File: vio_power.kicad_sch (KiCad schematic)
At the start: 55 parts, among them J29 292161-3, U41 TCA6408ARGTR, U42 AZ1117H-1.8TRE1_SOT223, U43 LP2985-3.3, U44 MCP4728, U45 TPS7A4501DCQR, U46 TPS7A4501DCQR

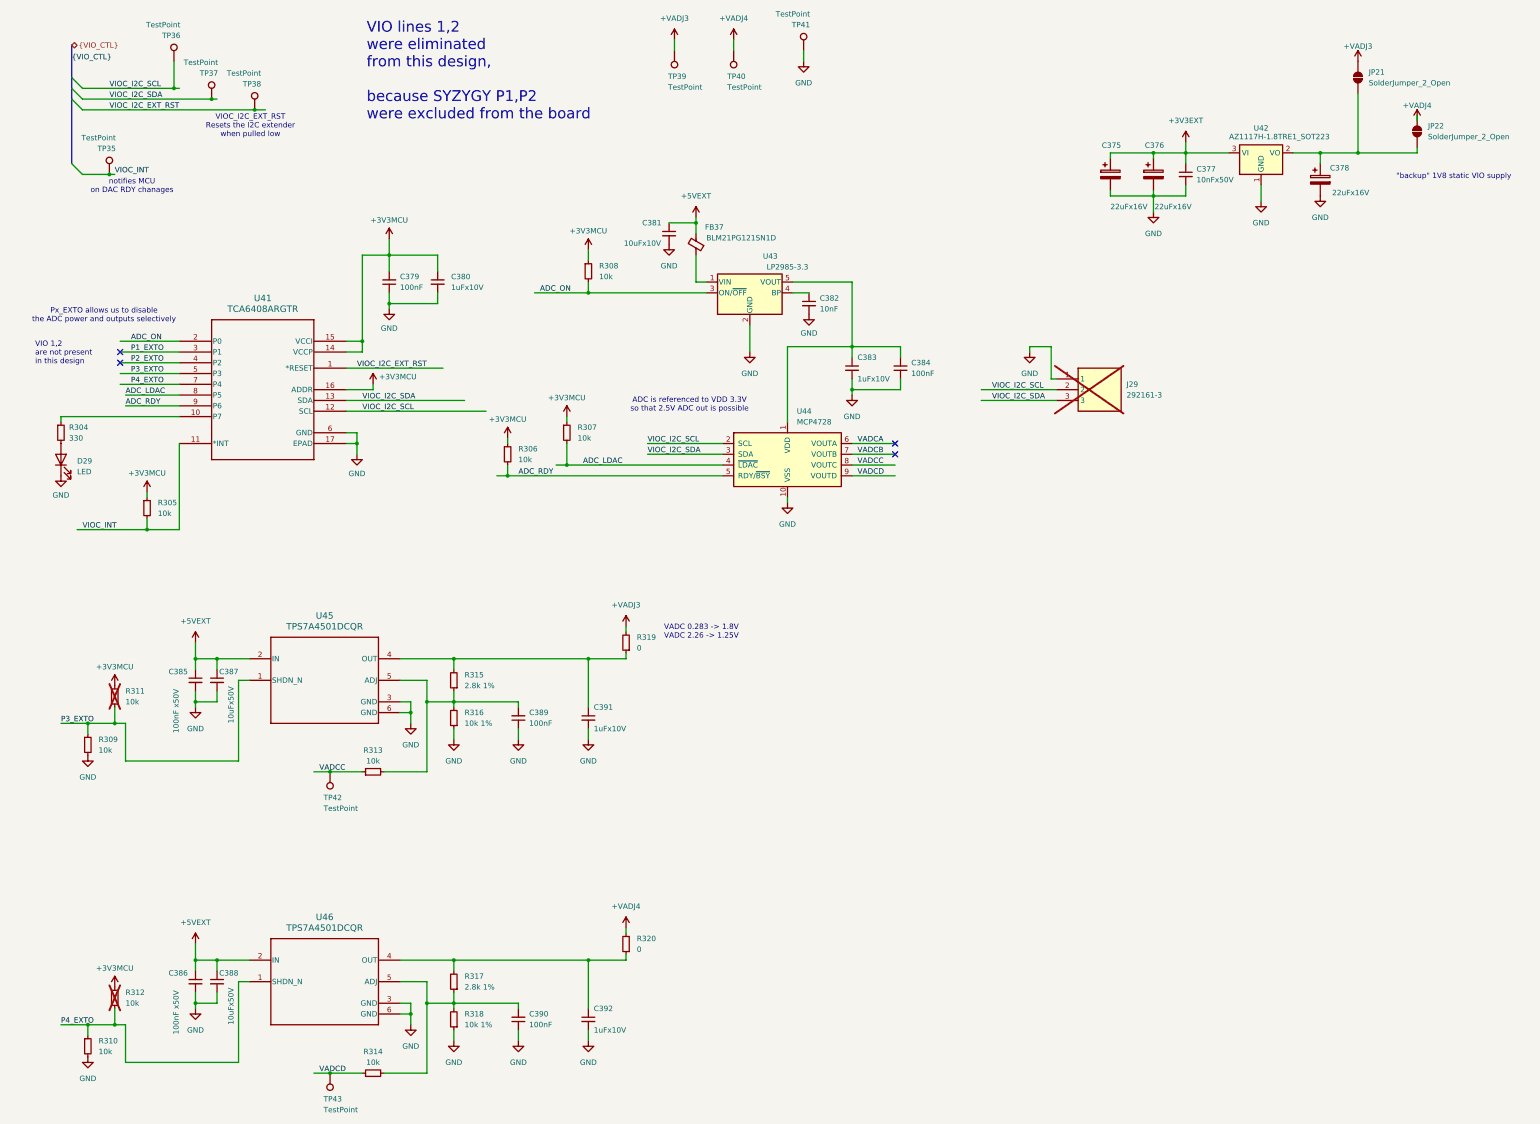
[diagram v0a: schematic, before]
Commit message: ver. bump to D 0.9.9, VIO is powered from U42 by default
The schema version has been updated to D 0.9.9
Resistors R396 and R397 in VIO Power sheet are connecting a 1.8V LDO U42 to the VIO by default.
Schema pdf is updated with the latest version.
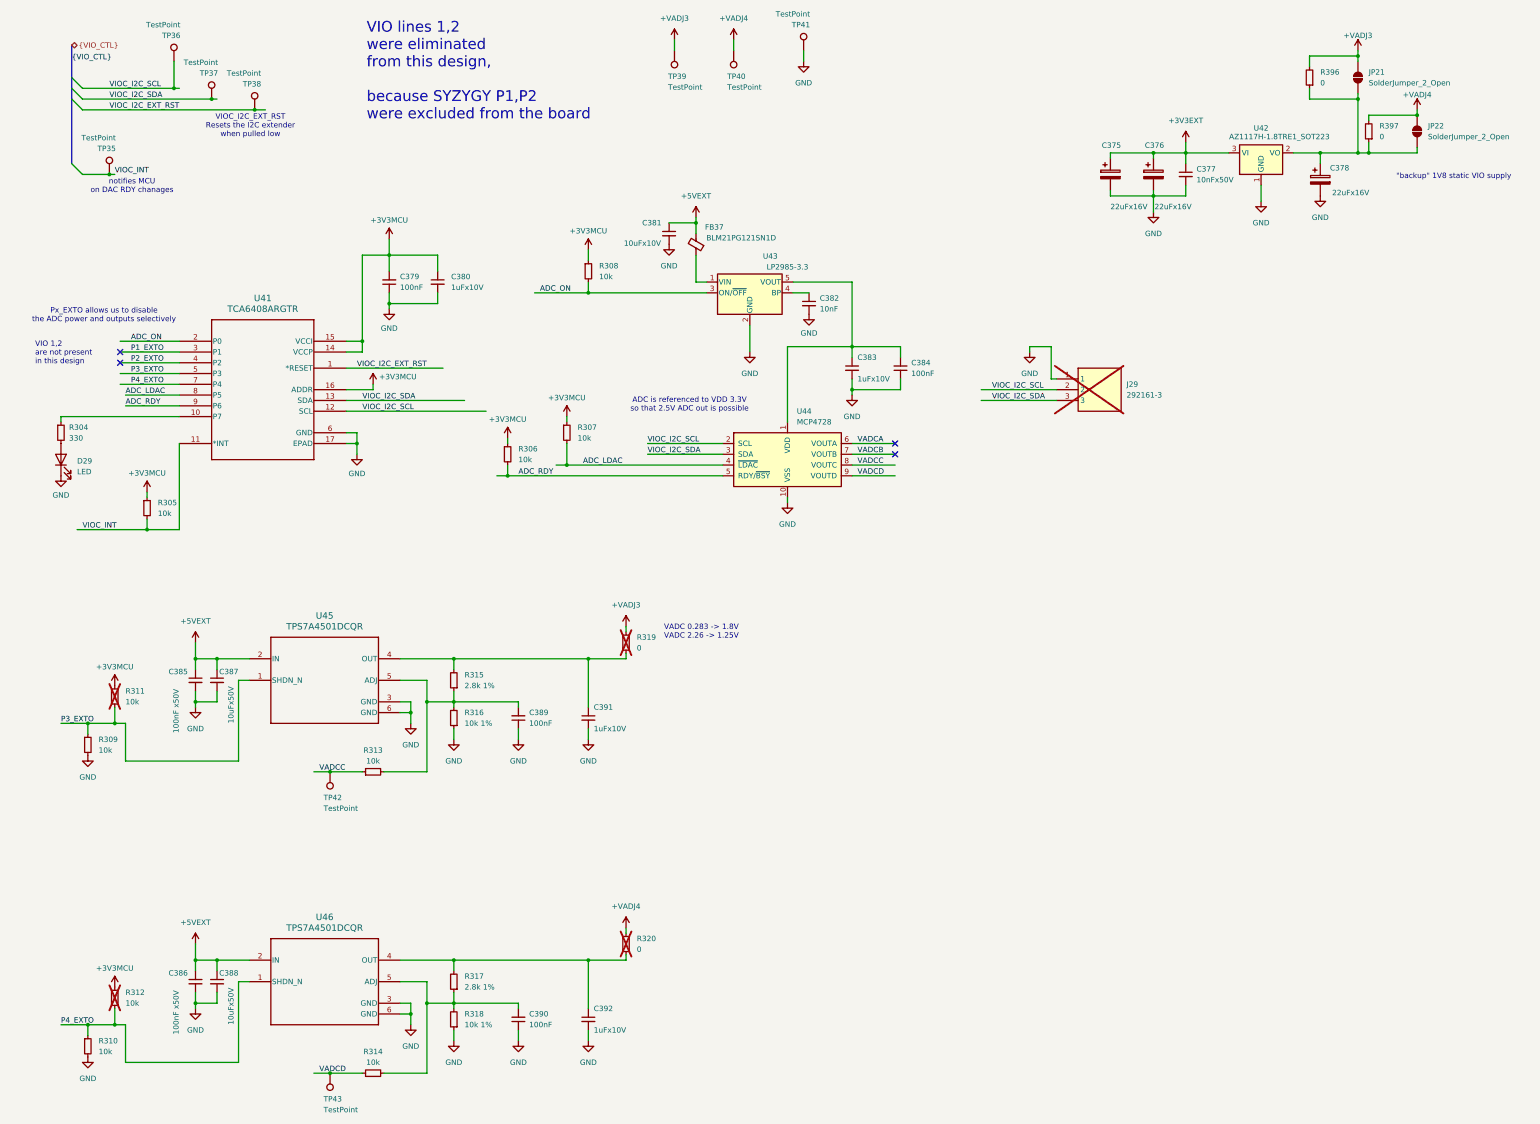
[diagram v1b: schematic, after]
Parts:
- added R396, R397: 0, Resistor_SMD:R_0805_2012Metric, symbol Device:R_Small
- R319, R320: now not fitted
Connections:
- net +VADJ3: now also R396.2
- net +VADJ4: now also R397.2
- net at C378.1, JP21.1 (A), JP22.1 (A)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: now also R396.1, R397.1

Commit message: JLCPCB ID attribute updates
These 'JLCPCB Part #' updates reflect the JLCPCB assembly order # SMT026073061946-2250854A
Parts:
- R315, R317: JLCPCB Part # C62741 -> C409906; Part 0402WGF2801TCE -> ERJ2RKF2801X
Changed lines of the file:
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@@
 			)
 		)
-		(property "Description" "-55℃~+155℃ 2.8kΩ 50V 62.5mW Thick Film Resistor ±1% ±100ppm/℃ 0402 Chip Resistor - Surface Mount ROHS"
+		(property "Description" "-55℃~+155℃ 100V 100mW 2.8kΩ Thick Film Resistor ±1% ±100ppm/℃ 0402 Chip Resistor - Surface Mount ROHS"
 			(at 114.3 250.19 0)
 			(effects
@@
 			)
 		)
-		(property "JLCPCB Part #" "C62741"
+		(property "JLCPCB Part #" "C409906"
 			(at 114.3 250.19 0)
 			(effects
@@
 			)
 		)
-		(property "Part" "0402WGF2801TCE"
+		(property "Part" "ERJ2RKF2801X"
 			(at 114.3 250.19 0)
 			(effects
@@
 			)
 		)
-		(property "Description" "-55℃~+155℃ 2.8kΩ 50V 62.5mW Thick Film Resistor ±1% ±100ppm/℃ 0402 Chip Resistor - Surface Mount ROHS"
-			(at 114.3 179.07 0)
-			(effects
-				(font
-					(size 1.27 1.27)
-				)
-				(hide yes)
-			)
-		)
-		(property "JLCPCB Part #" "C62741"
-			(at 114.3 179.07 0)
-			(effects
-				(font
-					(size 1.27 1.27)
-				)
-				(hide yes)
-			)
-		)
-		(property "Part" "0402WGF2801TCE"
-			(at 114.3 179.07 0)
-			(effects
+		(property "Description" "-55℃~+155℃ 100V 100mW 2.8kΩ Thick Film Resistor ±1% ±100ppm/℃ 0402 Chip Resistor - Surface Mount ROHS"
+			(at 114.3 179.07 0)
+			(effects
+				(font
+					(size 1.27 1.27)
+				)
+				(hide yes)
+			)
+		)
+		(property "JLCPCB Part #" "C409906"
+			(at 114.3 179.07 0)
+			(effects
+				(font
+					(size 1.27 1.27)
+				)
+				(hide yes)
+			)
+		)
+		(property "Part" "ERJ2RKF2801X"
+			(at 114.3 179.07 0)
+			(effects
